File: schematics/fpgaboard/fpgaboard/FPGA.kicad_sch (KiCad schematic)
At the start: 11 parts, among them J1 SODIMM-200, U1 LFE5UM-85F-8BG381I, U13 W25Q32JVSS

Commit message: Some work on FPGA board, adding some decoupling, SODIMM signals etc.
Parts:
- added C4: C_Small, Capacitor_SMD:C_0402_1005Metric, symbol Device:C_Small
- C1, C2, C3: footprint Capacitor_SMD:C_0201_0603Metric -> Capacitor_SMD:C_0402_1005Metric
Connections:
- net PT29B is gone; now on net S1: J1.41
- net GND: now also C4.2
- net IO_3v3: now also C4.1
- net RAM_D16: now also U1.C15 (PT105B); no longer U1.B15 (PT105A)
- net RAM_D17: now also U1.B15 (PT105A); no longer U1.C15 (PT105B)
- net S3: now reaches U1.R1 (PB4A)
- net S3: now also J1.51
- net S4: now reaches U1.T1 (PB4B)
- net S4: now also J1.57
- net S5: now reaches U1.U1 (PB6A)
- net S5: now also J1.59
- net S6: now reaches U1.V1 (PB6B)
- net S6: now also J1.61
- net S1: now reaches U1.N1 (PL89D)
- net S2: now reaches U1.P1 (PL92A)
- net S2: now also J1.49
- net S80: now reaches J1.100
- net S26: now reaches J1.101
- net S81: now reaches J1.102
- net S27: now reaches J1.103
- net S82: now reaches J1.104
- net S28: now reaches J1.109
- net S83: now reaches J1.110
- net S29: now reaches J1.111
- net S84: now reaches J1.112
- net S30: now reaches J1.113
- net S85: now reaches J1.114
- net S31: now reaches J1.115
- net S86: now reaches J1.116
- net S32: now reaches J1.117
- net S87: now reaches J1.118
- net S33: now reaches J1.119
- net S88: now reaches J1.120
- net S34: now reaches J1.121
- net S89: now reaches J1.122
- net S35: now reaches J1.123
- net S90: now reaches J1.124
- net S36: now reaches J1.125
- net S91: now reaches J1.126
- net S37: now reaches J1.127
- net S92: now reaches J1.128
- net S38: now reaches J1.129
- net S93: now reaches J1.130
- net S39: now reaches J1.131
- net S94: now reaches J1.132
- net S40: now reaches J1.133
- net S95: now reaches J1.134
- net S41: now reaches J1.135
- net S96: now reaches J1.136
- net S42: now reaches J1.137
- net S97: now reaches J1.138
- net S43: now reaches J1.139
- net S98: now reaches J1.140
- net S44: now reaches J1.141
- net S99: now reaches J1.142
- net S45: now reaches J1.143
- net S100: now reaches J1.144
- net S46: now reaches J1.145
- net S101: now reaches J1.146
- net S47: now reaches J1.147
- net S102: now reaches J1.148
- net S48: now reaches J1.149
- net S103: now reaches J1.150
- net S49: now reaches J1.151
- net S104: now reaches J1.152
- net S50: now reaches J1.153
- net S105: now reaches J1.154
- net S51: now reaches J1.155
- net S106: now reaches J1.156
- net S52: now reaches J1.42
- net S53: now reaches J1.44
- net S54: now reaches J1.46
- net S55: now reaches J1.48
- net S56: now reaches J1.50
- net S57: now reaches J1.52
- net S58: now reaches J1.54
- net S59: now reaches J1.58
- net S60: now reaches J1.60
- net S61: now reaches J1.62
- net S7: now reaches J1.63
- net S62: now reaches J1.64
- net S8: now reaches J1.65
- net S63: now reaches J1.66
- net S9: now reaches J1.67
- net S64: now reaches J1.68
- net S10: now reaches J1.69
- net S65: now reaches J1.70
- net S11: now reaches J1.71
- net S66: now reaches J1.72
- net S12: now reaches J1.73
- net S67: now reaches J1.74
- net S13: now reaches J1.75
- net S68: now reaches J1.76
- net S14: now reaches J1.77
- net S69: now reaches J1.78
- net S15: now reaches J1.79
- net S70: now reaches J1.80
- net S16: now reaches J1.81
- net S71: now reaches J1.82
- net S17: now reaches J1.83
- net S72: now reaches J1.84
- net S18: now reaches J1.85
- net S73: now reaches J1.86
- net S19: now reaches J1.87
- net S74: now reaches J1.88
- net S20: now reaches J1.89
- net S75: now reaches J1.90
- net S21: now reaches J1.91
- net S76: now reaches J1.92
- net S22: now reaches J1.93
- net S77: now reaches J1.94
- net S23: now reaches J1.95
- net S78: now reaches J1.96
- net S24: now reaches J1.97
- net S79: now reaches J1.98
- net S25: now reaches J1.99
- no-connect marks 26 -> 70

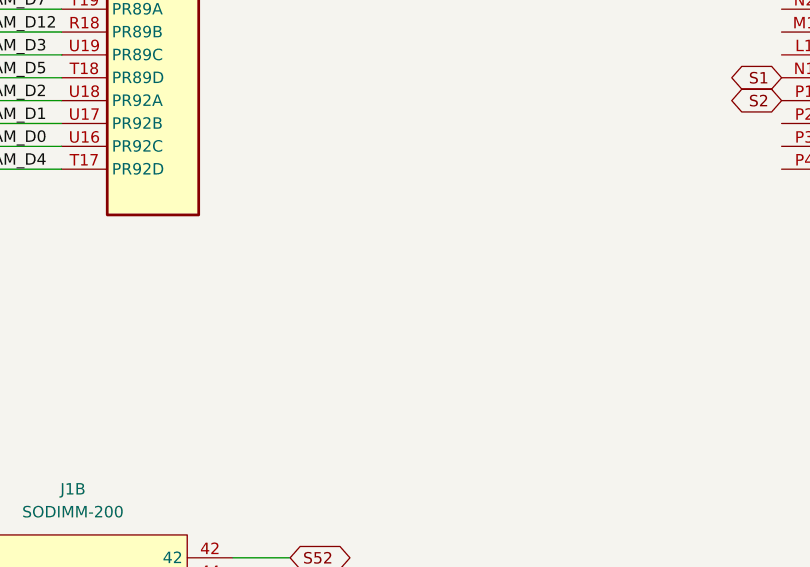
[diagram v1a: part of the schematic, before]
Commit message: FPGA board update; using 6 layer setup and "via in pad".
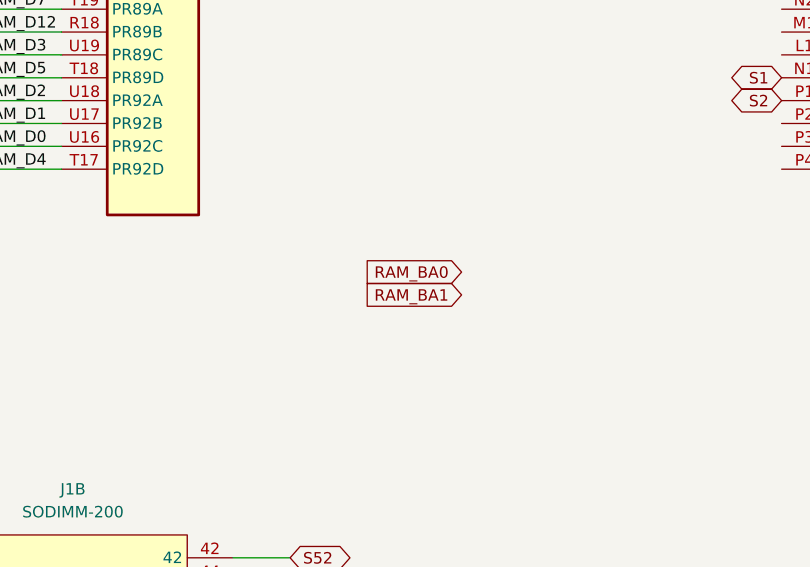
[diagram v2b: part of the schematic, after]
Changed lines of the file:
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@@
+		)
+	)
+	(global_label "RAM_BA0"
+		(shape input)
+		(at 308.61 140.97 180)
+		(fields_autoplaced yes)
+		(effects
+			(font
+				(size 1.27 1.27)
+			)
+			(justify right)
+		)
+		(property "Intersheetrefs" "${INTERSHEET_REFS}"
+			(at 297.2791 140.97 0)
+			(effects
+				(font
+					(size 1.27 1.27)
+				)
+				(justify right)
+				(hide yes)
+			)
 		)
 	)
@@
 			(effects
 				(font
+					(size 1.27 1.27)
+				)
+				(justify right)
+				(hide yes)
+			)
+		)
+	)
+	(global_label "RAM_BA1"
+		(shape input)
+		(at 308.61 143.51 180)
+		(fields_autoplaced yes)
+		(effects
+			(font
+				(size 1.27 1.27)
+			)
+			(justify right)
+		)
+		(property "Intersheetrefs" "${INTERSHEET_REFS}"
+			(at 297.2791 143.51 0)
+			(effects
+				(font

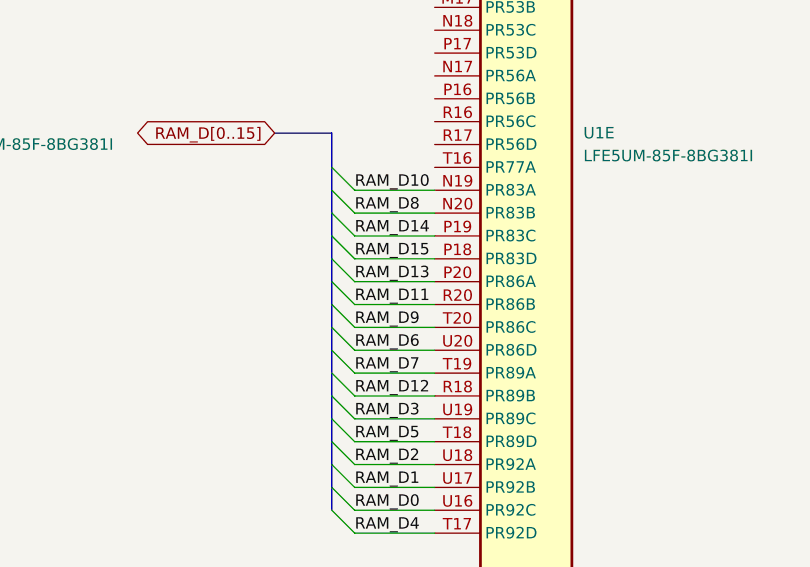
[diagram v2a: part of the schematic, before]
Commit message: Rerouting some wires on FPGA board.
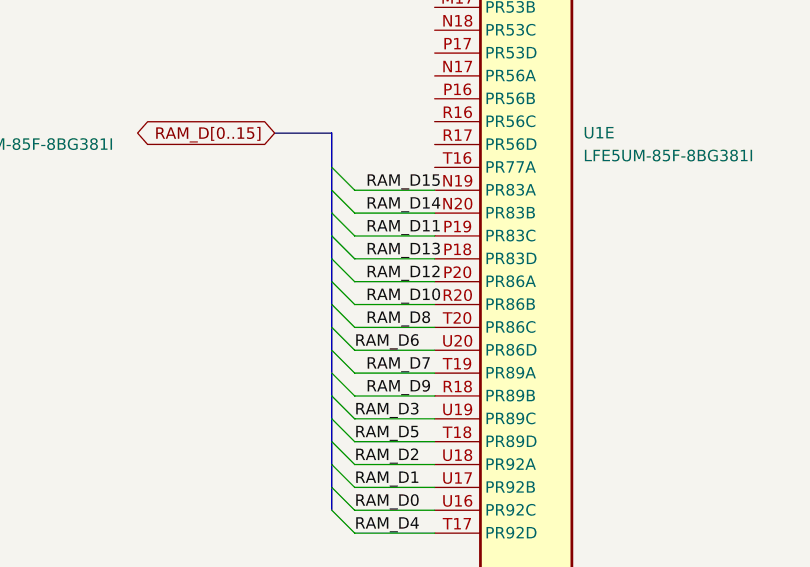
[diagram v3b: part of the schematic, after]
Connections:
- net RAM_D10: now also U1.R20 (PR86B); no longer U1.N19 (PR83A)
- net RAM_D11: now also U1.P19 (PR83C); no longer U1.R20 (PR86B)
- net RAM_D12: now also U1.P20 (PR86A); no longer U1.R18 (PR89B)
- net RAM_D13: now also U1.P18 (PR83D); no longer U1.P20 (PR86A)
- net RAM_D14: now also U1.N20 (PR83B); no longer U1.P19 (PR83C)
- net RAM_D15: now also U1.N19 (PR83A); no longer U1.P18 (PR83D)
- net RAM_D8: now also U1.T20 (PR86C); no longer U1.N20 (PR83B)
- net RAM_D9: now also U1.R18 (PR89B); no longer U1.T20 (PR86C)
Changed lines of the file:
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@@
 	)
 	(label "RAM_D8"
-		(at 255.27 93.98 0)
+		(at 256.54 106.68 0)
 		(effects
 			(font
@@
 	)
 	(label "RAM_D9"
-		(at 255.27 106.68 0)
+		(at 256.54 114.3 0)
 		(effects
 			(font
@@
 	)
 	(label "RAM_D14"
-		(at 255.27 96.52 0)
+		(at 256.54 93.98 0)
 		(effects
 			(font
@@
 	)
 	(label "RAM_D13"
-		(at 255.27 101.6 0)
+		(at 256.54 99.06 0)
 		(effects
 			(font
@@
 	)
 	(label "RAM_D12"
-		(at 255.27 114.3 0)
+		(at 256.54 101.6 0)
 		(effects
 			(font
@@
 	)
 	(label "RAM_D10"
-		(at 255.27 91.44 0)
+		(at 256.54 104.14 0)
 		(effects
 			(font
@@
 	)
 	(label "RAM_D7"
-		(at 255.27 111.76 0)
+		(at 256.54 111.76 0)
 		(effects
 			(font
@@
 	)
 	(label "RAM_D11"
-		(at 255.27 104.14 0)
+		(at 256.54 96.52 0)
 		(effects
 			(font
@@
 	)
 	(label "RAM_D15"
-		(at 255.27 99.06 0)
-		(effects
-			(font
+		(at 256.54 91.44 0)
+		(effects
+			(font

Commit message: More work on FPGA board.
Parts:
- added C5, C6, C7: C_Small, Capacitor_SMD:C_0402_1005Metric, symbol Device:C_Small
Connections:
- net GND: now also C5.2, C6.2, C7.2
- net IO_3v3: now also C5.1, C6.1, C7.1
- net RAM_BA0: now also U1.L18 (PR50C)
- net RAM_BA1: now also U1.M18 (PR50D)
- net S10: now also U1.C2 (PL35D)
- net S11: now also U1.D1 (PL38B)
- net S12: now also U1.D2 (PL38C)
- net S13: now also U1.E1 (PL38D)
- net S14: now also U1.E2 (PL44D)
- net S15: now also U1.F1 (PL47B)
- net S16: now also U1.F2 (PL44C)
- net S17: now also U1.G1 (PL47D)
- net S18: now also U1.G2 (PL47A)
- net S19: now also U1.H1 (PL53C)
- net S20: now also U1.H2 (PL47C)
- net S21: now also U1.J1 (PL53B)
- net S22: now also U1.J3 (PL50C)
- net S23: now also U1.K1 (PL53D)
- net S24: now also U1.K2 (PL53A)
- net S5: now also U1.A2 (PL35A); no longer U1.U1 (PB6A)
- net S6: now also U1.A3 (PL14C); no longer U1.V1 (PB6B)
- net S7: now also U1.B1 (PL35B)
- net S8: now also U1.B2 (PL35C)
- net S9: now also U1.C1 (PL38A)
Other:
- moved on the sheet: C1, C2, C3, C4, C48, U13, U1B, U1C, U1D, U1E, U1F, U1G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

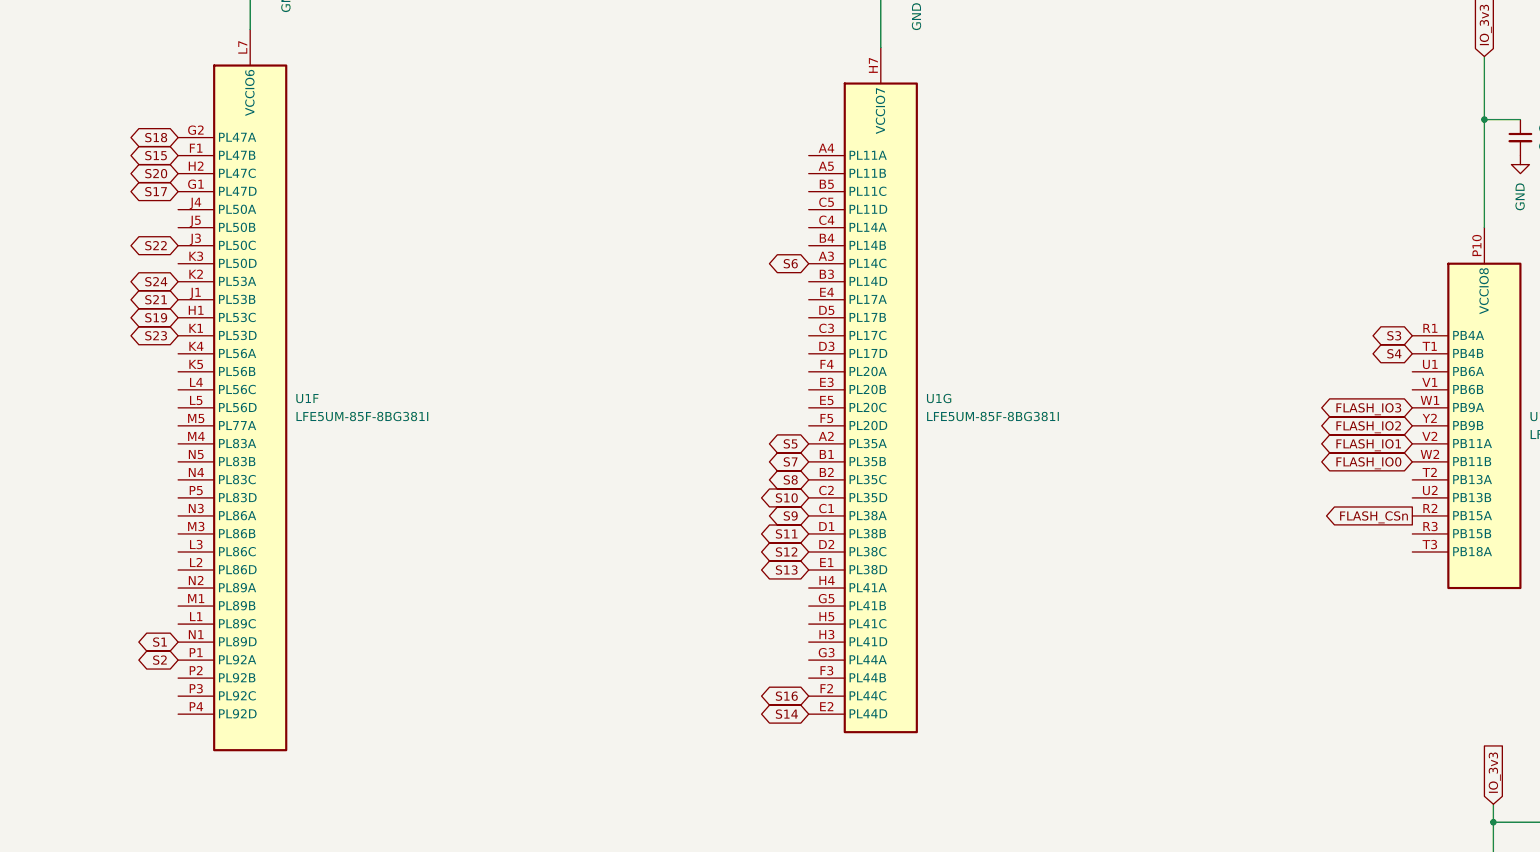
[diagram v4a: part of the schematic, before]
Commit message: Top row of SODIMM wired up to FPGA in fpga board.
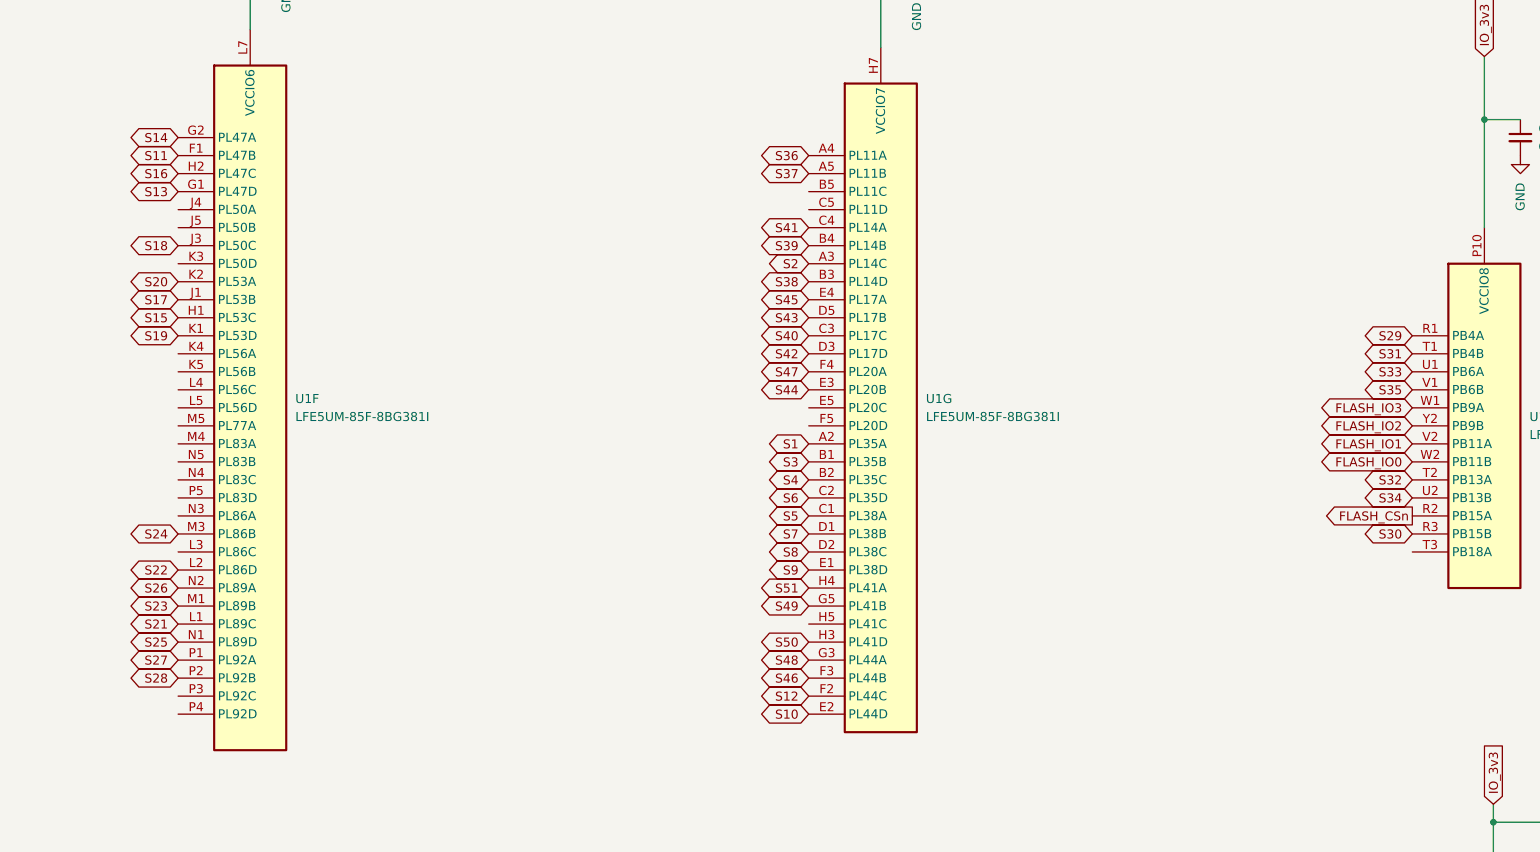
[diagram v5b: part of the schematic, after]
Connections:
- net S1: now also U1.A2 (PL35A); no longer U1.N1 (PL89D)
- net S10: now also U1.E2 (PL44D); no longer U1.C2 (PL35D)
- net S11: now also U1.F1 (PL47B); no longer U1.D1 (PL38B)
- net S12: now also U1.F2 (PL44C); no longer U1.D2 (PL38C)
- net S13: now also U1.G1 (PL47D); no longer U1.E1 (PL38D)
- net S14: now also U1.G2 (PL47A); no longer U1.E2 (PL44D)
- net S15: now also U1.H1 (PL53C); no longer U1.F1 (PL47B)
- net S16: now also U1.H2 (PL47C); no longer U1.F2 (PL44C)
- net S17: now also U1.J1 (PL53B); no longer U1.G1 (PL47D)
- net S18: now also U1.J3 (PL50C); no longer U1.G2 (PL47A)
- net S19: now also U1.K1 (PL53D); no longer U1.H1 (PL53C)
- net S2: now also U1.A3 (PL14C); no longer U1.P1 (PL92A)
- net S20: now also U1.K2 (PL53A); no longer U1.H2 (PL47C)
- net S21: now also U1.L1 (PL89C); no longer U1.J1 (PL53B)
- net S22: now also U1.L2 (PL86D); no longer U1.J3 (PL50C)
- net S23: now also U1.M1 (PL89B); no longer U1.K1 (PL53D)
- net S24: now also U1.M3 (PL86B); no longer U1.K2 (PL53A)
- net S25: now also U1.N1 (PL89D)
- net S26: now also U1.N2 (PL89A)
- net S27: now also U1.P1 (PL92A)
- net S28: now also U1.P2 (PL92B)
- net S29: now also U1.R1 (PB4A)
- net S3: now also U1.B1 (PL35B); no longer U1.R1 (PB4A)
- net S30: now also U1.R3 (PB15B)
- net S31: now also U1.T1 (PB4B)
- net S32: now also U1.T2 (PB13A)
- net S33: now also U1.U1 (PB6A)
- net S34: now also U1.U2 (PB13B)
- net S35: now also U1.V1 (PB6B)
- net S36: now also U1.A4 (PL11A)
- net S37: now also U1.A5 (PL11B)
- net S38: now also U1.B3 (PL14D)
- net S39: now also U1.B4 (PL14B)
- net S4: now also U1.B2 (PL35C); no longer U1.T1 (PB4B)
- net S40: now also U1.C3 (PL17C)
- net S41: now also U1.C4 (PL14A)
- net S42: now also U1.D3 (PL17D)
- net S43: now also U1.D5 (PL17B)
- net S44: now also U1.E3 (PL20B)
- net S45: now also U1.E4 (PL17A)
- net S46: now also U1.F3 (PL44B)
- net S47: now also U1.F4 (PL20A)
- net S48: now also U1.G3 (PL44A)
- net S49: now also U1.G5 (PL41B)
- net S5: now also U1.C1 (PL38A); no longer U1.A2 (PL35A)
- net S50: now also U1.H3 (PL41D)
- net S51: now also U1.H4 (PL41A)
- net S6: now also U1.C2 (PL35D); no longer U1.A3 (PL14C)
- net S7: now also U1.D1 (PL38B); no longer U1.B1 (PL35B)
- net S8: now also U1.D2 (PL38C); no longer U1.B2 (PL35C)
- net S9: now also U1.E1 (PL38D); no longer U1.C1 (PL38A)
